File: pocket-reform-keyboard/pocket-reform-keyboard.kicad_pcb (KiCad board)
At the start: 2 copper layers, 160 x 70 mm, 137 parts, among them J1 USB, J2 UART, J3 AUX, SW1 Choc, SW10 Choc, SW11 Choc, SW12 Choc, SW13 Choc, SW14 Choc, SW15 Choc, SW16 Choc, SW17 Choc, SW18 Choc, SW19 Choc, SW2 Choc, SW20 Choc, SW21 Choc, SW22 Choc, SW23 Choc, SW24 Choc, SW25 Choc, SW26 Choc, SW27 Choc, SW28 Choc, SW29 Choc, SW3 Choc, SW30 Choc, SW31 Choc, SW32 Choc, SW33 Choc, SW34 Choc, SW35 Choc, SW36 Choc, SW37 Choc, SW38 Choc, SW39 Choc, SW4 Choc, SW40 Choc, SW41 Choc, SW42 Choc, SW43 Choc, SW44 Choc, SW45 Choc, SW46 Choc, SW47 Choc, SW48 Choc, SW49 Choc, SW5 Choc, SW50 Choc, SW51 Choc, SW52 Choc, SW53 Choc, SW54 Choc, SW55 Choc, SW56 RESET, SW6 Choc, SW7 Choc, SW8 Choc, SW9 Choc, U1 MCP1700-3302E_SOT23, U2 ATMEGA32U4-AU, Y1 16MHz

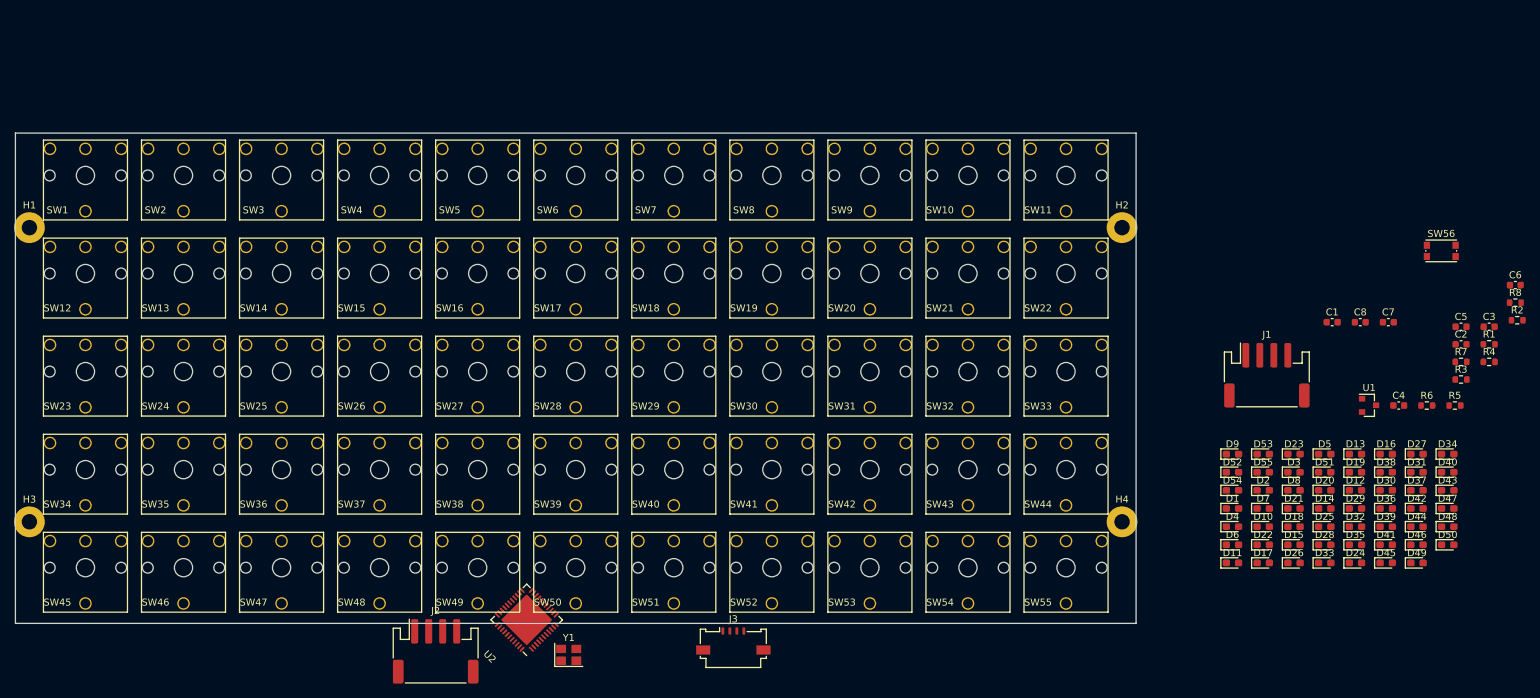
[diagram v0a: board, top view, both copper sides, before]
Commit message: keyboard: first routed draft
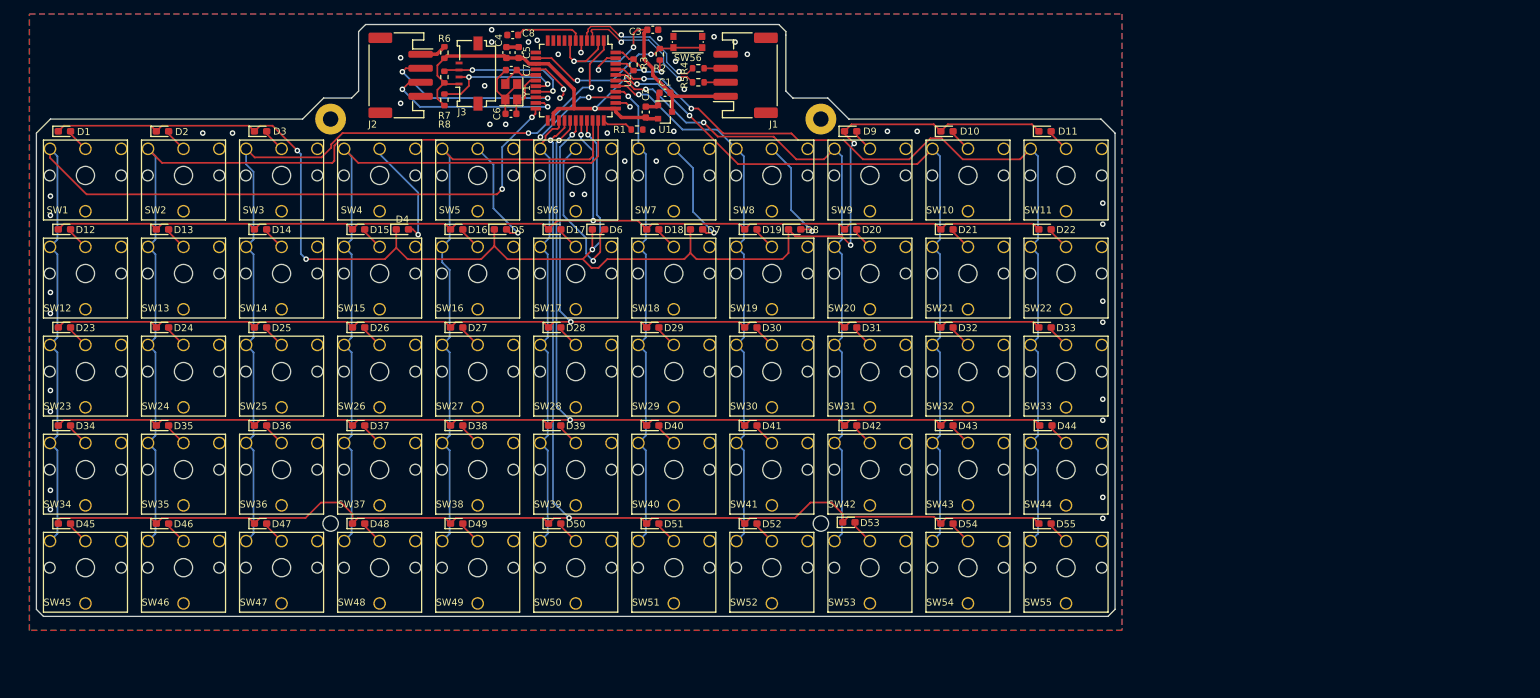
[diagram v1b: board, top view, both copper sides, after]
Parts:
- added G***: LOGO, footprints:pocket-reform, B.Cu at (135.8, 61.5)
- H3, H4: footprint MountingHole:MountingHole_2.2mm_M2_Pad -> MountingHole:MountingHole_2.2mm_M2
- U2: footprint Package_DFN_QFN:QFN-44-1EP_7x7mm_P0.5mm_EP5.15x5.15mm -> Package_QFP:TQFP-44_10x10mm_P0.8mm
- moved D34 197.5 mm to (63.0, 110.8)
- moved D45 188.8 mm to (63.0, 124.8)
- moved D12 188.1 mm to (63.0, 82.8)
- moved D46 179.1 mm to (77.0, 124.8)
- moved D23 176.5 mm to (63.0, 96.8)
- moved D1 175.2 mm to (63.0, 68.8)
- moved D24 173.6 mm to (77.0, 96.8)
- moved D13 173.3 mm to (77.0, 82.8)
- moved D35 171.2 mm to (77.0, 110.8)
- moved D47 169.5 mm to (91.0, 124.8)
- moved D2 165.3 mm to (77.0, 68.8)
- moved D36 161.2 mm to (91.0, 110.8)
- moved D14 157.1 mm to (91.0, 82.8)
- moved R8 155.6 mm to (117.2, 64.2), turned to 90 degrees
- moved D48 155.5 mm to (105.0, 124.8)
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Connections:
- U2 pad 10: COL6 -> Net-(U2-Pad10)
- U2 pad 11: COL5 -> Net-(U2-Pad11)
- U2 pad 25: ROW6 -> COL6
- U2 pad 31: Net-(U2-Pad31) -> COL5
- U2 pad 37: Net-(U2-Pad37) -> COL7
- U2 pad 38: Net-(U2-Pad38) -> COL8
- U2 pad 39: COL11 -> COL9
- U2 pad 41: COL9 -> COL11
- U2 pad 8: COL8 -> Net-(U2-Pad8)
- U2 pad 9: COL7 -> Net-(U2-Pad9)
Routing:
- net ROW1: track 0.00 -> 219.8 mm, vias 0 -> 6
- net ROW5: track 0.00 -> 211.2 mm, vias 0 -> 2
- net ROW4: track 0.00 -> 191.1 mm, vias 0 -> 2
- net ROW3: track 0.00 -> 177.0 mm, vias 0 -> 2
- net ROW2: track 0.00 -> 162.5 mm, vias 0 -> 2
- net COL1: track 0.00 -> 141.3 mm, vias 0 -> 2
- net COL2: track 0.00 -> 132.2 mm, vias 0 -> 2
- net COL11: track 0.00 -> 127.2 mm, vias 0 -> 2
- net COL3: track 0.00 -> 121.4 mm, vias 0 -> 2
- net COL10: track 0.00 -> 110.9 mm, vias 0 -> 2
- net COL4: track 0.00 -> 102.1 mm
- net COL9: track 0.00 -> 96.0 mm, vias 0 -> 2
- net COL5: track 0.00 -> 87.0 mm
- net COL8: track 0.00 -> 80.5 mm, vias 0 -> 1
- net COL7: track 0.00 -> 69.9 mm, vias 0 -> 1
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- added copper zone on B.Cu, net GND
- added copper zone on F.Cu, net GND
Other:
- board size 160 x 70 mm -> 154 x 84.5 mm

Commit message: keyboard: D-1, sent to fab
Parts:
- added D56: LED_RGBA, footprints:LED_150080M153000, F.Cu at (123.2, 67.8)
- added GFX2: MNT, footprints:mpre-badge-d1, B.Cu at (153.9, 58.1)
- added R10: 47, Resistor_SMD:R_0603_1608Metric, F.Cu at (126.4, 68.4)
- added R11: 47, Resistor_SMD:R_0603_1608Metric, F.Cu at (119.9, 68.4)
- added R9: 220, Resistor_SMD:R_0603_1608Metric, F.Cu at (116.8, 68.4)
- GFX1: renamed from G***; value LOGO -> MNT
- moved GFX1 12.1 mm to (123.7, 60.5)
- moved SW56 0.20 mm to (152.0, 55.8)
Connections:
- net PWM renamed Net-(U2-Pad12)
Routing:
- net Net-(R9-Pad2): track 0.00 -> 40.8 mm, vias 0 -> 2
- net Net-(R11-Pad2): track 0.00 -> 39.0 mm, vias 0 -> 2
- net Net-(R10-Pad2): track 0.00 -> 17.2 mm, vias 0 -> 2
- net Net-(D56-Pad1): track 0.00 -> 12.7 mm, vias 0 -> 2
- net +3V3: track 69.8 -> 75.7 mm
- net Net-(D56-Pad3): track 0.00 -> 1.56 mm
- net Net-(D56-Pad2): track 0.00 -> 1.46 mm
- net COL3: track 121.4 -> 122.3 mm
- net /Pocket Reform Keyboard MCU/UD-: track 20.3 -> 19.5 mm
- net /Pocket Reform Keyboard MCU/UD+: track 20.6 -> 20.0 mm
